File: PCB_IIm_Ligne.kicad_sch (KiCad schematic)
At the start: 24 parts, among them J1 Screw_Terminal_01x08, J2 Screw_Terminal_01x08, J3 Screw_Terminal_01x02, K1 G2RK-2 DC12, K2 Relay_DPDT_Latching_2coil, Q1 IRFZ14, Q2 MPSA56, U2 NE555DR

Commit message: Schematic V1
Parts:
- removed J3: Screw_Terminal_01x02, TerminalBlock_Phoenix:TerminalBlock_Phoenix_MKDS-1,5-2_1x02_P5.00mm_Horizontal, symbol Connector:Screw_Terminal_01x02
- added J4: Screw_Terminal_01x08, TerminalBlock_Phoenix:TerminalBlock_Phoenix_MPT-0,5-8-2.54_1x08_P2.54mm_Horizontal, symbol Connector:Screw_Terminal_01x08
- added J5: Screw_Terminal_01x08, TerminalBlock_Phoenix:TerminalBlock_Phoenix_MKDS-1,5-8-5.08_1x08_P5.08mm_Horizontal, symbol Connector:Screw_Terminal_01x08
- J1, J2: footprint TerminalBlock_Phoenix:TerminalBlock_Phoenix_MKDS-1,5-8-5.08_1x08_P5.08mm_Horizontal -> TerminalBlock_Phoenix:TerminalBlock_Phoenix_MPT-0,5-8-2.54_1x08_P2.54mm_Horizontal
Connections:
- net LED_Traction is gone; now on net LED_Alim: J2.5 (Pin_5)
- net AlimBoutonSens: now also J4.6 (Pin_6)
- net GND: now also J2.2 (Pin_2), J2.3 (Pin_3), J2.4 (Pin_4), J4.1 (Pin_1), J5.1 (Pin_1), J5.2 (Pin_2); no longer J1.1 (Pin_1)
- net LED_Alim: no longer J2.2 (Pin_2)
- net LED_SensA: now also J2.6 (Pin_6); no longer J2.3 (Pin_3)
- net LED_SensB: now also J2.7 (Pin_7); no longer J2.4 (Pin_4)
- net LED_TractionEnService: now also J2.8 (Pin_8)
- net OUT_ARD: now also J4.5 (Pin_5); no longer J1.5 (Pin_5)
- net POT1: now also J4.2 (Pin_2); no longer J1.2 (Pin_2)
- net POT2: now also J4.3 (Pin_3); no longer J1.3 (Pin_3)
- net POT3: now also J4.4 (Pin_4); no longer J1.4 (Pin_4)
- net RAIL_1: now also J5.8 (Pin_8)
- net RAIL_2: now also J5.7 (Pin_7)
- net RelaiBistableSensA: now also J4.7 (Pin_7)
- net RelaiBistableSensB: now also J4.8 (Pin_8)
- net Traction_N: no longer J1.6 (Pin_6)
- net Traction_P: now also J5.3 (Pin_3), J5.4 (Pin_4); no longer J1.7 (Pin_7)
- net VCC: now also J1.8 (Pin_8), J5.5 (Pin_5), J5.6 (Pin_6)
- new net BoutonSensA: J1.5 (Pin_5)
- new net BoutonSensB: J1.4 (Pin_4)
- new net InterrupteurPot1: J1.6 (Pin_6)
- new net InterrupteurPot2: J1.7 (Pin_7)
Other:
- note added: "Connecteur Alimentation"
- note added: "Connecteur Control"
- note added: "Connecteur LED"
- note removed: "A Faire : Importer relai monostable Club Importer relai Bistable Club Importer relai bistable traction Importer Mosfet"
- moved on the sheet: D2, D3, D4, D5, K1, K2, Q2, R1, R2, R3, R5, R6

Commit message: Schematic V2 + BOM
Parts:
- removed C1: 100nF, PCM_JLCPCB:C_0805, symbol PCM_JLCPCB-Capacitors:0805,100nF
- removed C2: 1nF, PCM_JLCPCB:C_0805, symbol PCM_JLCPCB-Capacitors:0805,1nF
- removed D5: D, Diode_THT:D_DO-15_P10.16mm_Horizontal, symbol Device:D
- removed D6, D7: 1N4001W, PCM_JLCPCB:D_SOD-123FL, symbol PCM_JLCPCB-Diodes:General,1N4001W
- removed J5: Screw_Terminal_01x08, TerminalBlock_Phoenix:TerminalBlock_Phoenix_MKDS-1,5-8-5.08_1x08_P5.08mm_Horizontal, symbol Connector:Screw_Terminal_01x08
- removed Q1: IRFZ14, PCM_Package_TO_SOT_THT_AKL:TO-220-3_Vertical_GDS, symbol PCM_Transistor_MOSFET_AKL:IRFZ14
- removed R7: 1kΩ, PCM_JLCPCB:R_0402, symbol PCM_JLCPCB-Resistors:0402,1kΩ
- removed R8: 5.1kΩ, PCM_JLCPCB:R_0603, symbol PCM_JLCPCB-Resistors:0603,5.1kΩ
- removed U2: NE555DR, Package_DIP:DIP-8_W7.62mm_Socket, symbol PCM_JLCPCB-ICs:Timer, 555
- added C1, C5, C6: C100nF, Capacitor_THT:C_Rect_L7.5mm_W6.5mm_P5.00mm, symbol Device:C
- added C2: C1nF, Capacitor_THT:C_Rect_L7.5mm_W6.5mm_P5.00mm, symbol Device:C
- added C3, C4: C_Polarized, symbol Device:C_Polarized
- added D1: D, Diode_THT:D_DO-15_P10.16mm_Horizontal, symbol Device:D
- added J3: Screw_Terminal_01x08, TerminalBlock_Phoenix:TerminalBlock_Phoenix_MKDS-1,5-8-5.08_1x08_P5.08mm_Horizontal, symbol Connector:Screw_Terminal_01x08
- added OC1, OC2, OC3: 6N137, PCM_Package_DIP_AKL:DIP-8_W7.62mm_Socket_LongPads, symbol PCM_Optocoupler_Logic_AKL:6N137
- added Q1: STP80NF12, PCM_Package_TO_SOT_THT_AKL:TO-220-3_Vertical_GDS, symbol PCM_Transistor_MOSFET_AKL:STP80NF12
- added Q3, Q4: IRF9540N, PCM_Package_TO_SOT_THT_AKL:TO-220-3_Vertical_GDS, symbol PCM_Transistor_MOSFET_AKL:IRF9540N
- added R10, R11, R9: R100, Resistor_THT:R_Axial_DIN0207_L6.3mm_D2.5mm_P10.16mm_Horizontal, symbol PCM_Elektuur:R
- added R12, R13, R4, R8: R4.7k, Resistor_THT:R_Axial_DIN0207_L6.3mm_D2.5mm_P10.16mm_Horizontal, symbol PCM_Elektuur:R
- added R14, R15, R16: R, Resistor_THT:R_Axial_DIN0207_L6.3mm_D2.5mm_P10.16mm_Horizontal, symbol PCM_Elektuur:R
- added R7: R1k, Resistor_THT:R_Axial_DIN0207_L6.3mm_D2.5mm_P10.16mm_Horizontal, symbol PCM_Elektuur:R
- added U1: NE555DR, Package_DIP:DIP-8_W7.62mm_Socket, symbol PCM_JLCPCB-ICs:Timer, 555
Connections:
- net BoutonSensA is gone; now on net RelaiBistableSensB: J1.5 (Pin_5)
- net BoutonSensB is gone; now on net RelaiBistableSensA: J1.4 (Pin_4)
- net GATE: now also R9.1 (+)
- net GND: now also C1.2, C2.2, C3.2, C4.2, C5.2, C6.2, D1.2 (A), J3.1 (Pin_1), J3.2 (Pin_2), OC1.3, OC1.5 (GND), OC2.3, OC2.5 (GND), OC3.3, OC3.5 (GND), Q1.2 (D), R4.1 (+), R8.2 (-), U1.1 (GND); no longer D3.2 (A), D4.2 (A)
- net Interrupteur2: now also R4.2 (-)
- net OUT: now also R8.1 (+), U1.3 (OUT)
- net OUT_ARD: now also R16.1 (+); no longer JP1.3 (B)
- net POT1: now also D3.1 (K)
- net POT2: now also D4.2 (A)
- net POT3: now also C1.1, U1.2 (TRIG), U1.6 (THRES)
- net RAIL_1: now also J3.7 (Pin_7)
- net RAIL_2: now also J3.8 (Pin_8)
- net RelaiBistableSensA: now also J1.2 (Pin_2), Q3.2 (D)
- net RelaiBistableSensB: now also J1.3 (Pin_3), D1.1 (K), Q4.2 (D); no longer D3.1 (K), D4.1 (K)
- net Traction_N: now also Q1.3 (S)
- net Traction_P: now also C4.1, J3.3 (Pin_3), J3.4 (Pin_4)
- net VCC: now also C3.1, C5.1, C6.1, J3.5 (Pin_5), J3.6 (Pin_6), OC1.7 (EN), OC1.8 (VCC), OC2.8 (VCC), OC3.8 (VCC), Q3.3 (S), Q4.3 (S), R12.2 (-), R13.2 (-), R7.1 (+), U1.4 (RST), U1.8 (VCC)
- new net: C2.1, U1.5 (CONT)
- new net: Q4.1 (G), R11.2 (-), R13.1 (+)
- new net: OC3.2, R16.2 (-)
- new net: Q1.1 (G), R9.2 (-)
- new net: D3.2 (A), D4.1 (K), R7.2 (-), U1.7 (DISCH)
- new net: Q3.1 (G), R10.2 (-), R12.1 (+)
- new net: OC2.2, R15.2 (-)
- new net: OC2.6, R11.1 (+)
- new net: OC1.2, R14.2 (-)
- new net: OC1.6, R10.1 (+)
- new net CommandeSensA: R14.1 (+)
- new net CommandeSensB: R15.1 (+)
- new net CommandeTractionArduino: JP1.3 (B), OC3.6
- no-connect marks 0 -> 2
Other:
- moved on the sheet: JP1, K2

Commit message: Schematic V1
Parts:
- removed C1: C100nF, Capacitor_THT:C_Rect_L7.5mm_W6.5mm_P5.00mm, symbol Device:C
- removed C2: C1nF, Capacitor_THT:C_Rect_L7.5mm_W6.5mm_P5.00mm, symbol Device:C
- removed OC2, OC3: 6N137, PCM_Package_DIP_AKL:DIP-8_W7.62mm_Socket_LongPads, symbol PCM_Optocoupler_Logic_AKL:6N137
- removed Q1: STP80NF12, PCM_Package_TO_SOT_THT_AKL:TO-220-3_Vertical_GDS, symbol PCM_Transistor_MOSFET_AKL:STP80NF12
- removed Q3, Q4: IRF9540N, PCM_Package_TO_SOT_THT_AKL:TO-220-3_Vertical_GDS, symbol PCM_Transistor_MOSFET_AKL:IRF9540N
- removed R16: R, Resistor_THT:R_Axial_DIN0207_L6.3mm_D2.5mm_P10.16mm_Horizontal, symbol PCM_Elektuur:R
- removed R9: R100, Resistor_THT:R_Axial_DIN0207_L6.3mm_D2.5mm_P10.16mm_Horizontal, symbol PCM_Elektuur:R
- removed U1: NE555DR, Package_DIP:DIP-8_W7.62mm_Socket, symbol PCM_JLCPCB-ICs:Timer, 555
- added C7: C100nF, Capacitor_THT:C_Rect_L7.5mm_W6.5mm_P5.00mm, symbol Device:C
- added C8: C_Polarized, symbol Device:C_Polarized
- added DZ1: 1N4733A, PCM_Diode_THT_AKL:D_DO-41_SOD81_P10.16mm_Horizontal_Zener, symbol PCM_Diode_Zener_AKL:1N4733A
- added JP2: SolderJumper_2_Bridged, Jumper:SolderJumper-2_P1.3mm_Bridged_RoundedPad1.0x1.5mm, symbol Jumper:SolderJumper_2_Bridged
- added Q3, Q4: BC557B, PCM_Package_TO_SOT_THT_AKL:TO-92_Inline_Wide_CBE, symbol PCM_Transistor_BJT_AKL:BC557B
- added Q5: 2N3904, PCM_Package_TO_SOT_THT_AKL:TO-92_Inline_Wide_EBC, symbol PCM_Transistor_BJT_AKL:2N3904
- added Q6: IRF40B207, PCM_Package_TO_SOT_THT_AKL:TO-220-3_Vertical_GDS, symbol PCM_Transistor_MOSFET_AKL:IRF40B207
- added U2: TLC555xP, PCM_Package_DIP_AKL:DIP-8_W7.62mm_LongPads, symbol Timer:TLC555xP
- C6: value C100nF -> C1nF
- OC1: footprint PCM_Package_DIP_AKL:DIP-8_W7.62mm_Socket_LongPads -> PCM_Package_DIP_AKL:DIP-8_W7.62mm_LongPads
- R10, R11: value R100 -> R
- R12, R8: value R4.7k -> R1k
- R13: value R4.7k -> R10k
- R14: value R -> R10k
- R15: value R -> R100
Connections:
- net CommandeSensB is gone; now on an unnamed net: R15.1 (+)
- net GND: now also J3.7 (Pin_7), J3.8 (Pin_8), R13.1 (+), C7.2, C8.2, DZ1.2 (A), U2.1 (GND); no longer J3.1 (Pin_1), J3.2 (Pin_2), OC1.3, R8.2 (-)
- net OUT: no longer R8.1 (+)
- net POT3: now also C5.1, U2.2 (TR), U2.6 (THR)
- net RAIL_1: now also J3.6 (Pin_6); no longer J3.7 (Pin_7)
- net RAIL_2: now also J3.5 (Pin_5); no longer J3.8 (Pin_8)
- net RelaiBistableSensA: now also Q3.1 (C)
- net RelaiBistableSensB: now also Q4.1 (C)
- net Traction_P: now also Q6.3 (S); no longer J3.3 (Pin_3), J3.4 (Pin_4)
- net VCC: now also J3.1 (Pin_1), J3.2 (Pin_2), R14.2 (-), R8.1 (+), C7.1, C8.1, Q3.3 (E), Q4.3 (E), Q5.3 (C), U2.4 (R), U2.8 (VCC); no longer C5.1, C6.1, J3.5 (Pin_5), J3.6 (Pin_6), OC1.7 (EN), OC1.8 (VCC), R12.2 (-), R13.2 (-)
- net at R11.2 (-): now also Q4.2 (B); no longer R13.1 (+)
- net at D3.2 (A), D4.1 (K), R7.2 (-): now also U2.7 (DIS)
- net at R12.1 (+): now also OC1.6; no longer R10.2 (-)
- net at R15.2 (-): now also Q6.1 (G)
- net CommandeRelaiArdB: now reaches R11.1 (+)
- net at OC1.2: no longer R14.2 (-)
- net CommandeRelaiArdA: now reaches R10.1 (+)
- net CommandeRelaiArdA: no longer OC1.6
- net CommandeSensA: no longer names the net of R14.1 (+)
- net CommandeSensA: now also Q5.1 (E)
- net Traction_N: no longer names the net of K1.3
- net Traction_N: no longer K1.6
- new net: C6.1, U2.5 (CV)
- new net: Q5.2 (B), R12.2 (-), R13.2 (-)
- new net: Q3.2 (B), R10.2 (-)
- new net: JP2.1 (A), OC1.7 (EN)
- new net +20V: J3.3 (Pin_3), J3.4 (Pin_4), Q6.2 (D)
- new net +5V: DZ1.1 (K), JP2.2 (B), OC1.8 (VCC), R8.2 (-)
- no-connect marks 2 -> 0
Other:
- note added: "Commande Relai Via Arduino - Transistor P"
- moved on the sheet: D3, D4, J3, R7

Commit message: Schematic V2
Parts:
- removed DZ1: 1N4733A, PCM_Diode_THT_AKL:D_DO-41_SOD81_P10.16mm_Horizontal_Zener, symbol PCM_Diode_Zener_AKL:1N4733A
- removed JP2: SolderJumper_2_Bridged, Jumper:SolderJumper-2_P1.3mm_Bridged_RoundedPad1.0x1.5mm, symbol Jumper:SolderJumper_2_Bridged
- removed OC1: 6N137, PCM_Package_DIP_AKL:DIP-8_W7.62mm_LongPads, symbol PCM_Optocoupler_Logic_AKL:6N137
- removed R8: R1k, Resistor_THT:R_Axial_DIN0207_L6.3mm_D2.5mm_P10.16mm_Horizontal, symbol PCM_Elektuur:R
- added H1, H2, H3, H4: MountingHole, MountingHole:MountingHole_3.2mm_M3, symbol Mechanical:MountingHole
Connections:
- net GND: now also K1.3, K1.6
- net CommandetTraction: now reaches U2.3 (Q)
- net CommandetTraction: now also R12.1 (+)
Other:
- moved on the sheet: R7

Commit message: Schematic V1
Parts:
- removed C8: C_Polarized, symbol Device:C_Polarized
- removed Q3, Q4: BC557B, PCM_Package_TO_SOT_THT_AKL:TO-92_Inline_Wide_CBE, symbol PCM_Transistor_BJT_AKL:BC557B
- removed Q5: 2N3904, PCM_Package_TO_SOT_THT_AKL:TO-92_Inline_Wide_EBC, symbol PCM_Transistor_BJT_AKL:2N3904
- removed R11: R, Resistor_THT:R_Axial_DIN0207_L6.3mm_D2.5mm_P10.16mm_Horizontal, symbol PCM_Elektuur:R
- removed R3: R4.7k, Resistor_THT:R_Axial_DIN0207_L6.3mm_D2.5mm_P10.16mm_Horizontal, symbol PCM_Elektuur:R
- added JP3, JP4: SolderJumper_2_Bridged, symbol Jumper:SolderJumper_2_Bridged
- added Q7, Q8, Q9: 2N2222A, PCM_Package_TO_SOT_THT_AKL:TO-92_Inline_Wide_EBC, symbol PCM_Transistor_BJT_AKL:2N3904
- added R18, R9: 260, Resistor_THT:R_Axial_DIN0207_L6.3mm_D2.5mm_P10.16mm_Horizontal, symbol PCM_Elektuur:R
- added R19, R8: 10k, Resistor_THT:R_Axial_DIN0207_L6.3mm_D2.5mm_P10.16mm_Horizontal, symbol PCM_Elektuur:R
- C5: value C100nF -> 270nF
- C7: value C100nF -> 100nF
- R10: value R -> 10k
- R12: value R1k -> 1K
- R15: value R100 -> 1K
- R4: value R4.7k -> 220
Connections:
- net CommandeRelaiArdA is gone; now on net GND: R10.1 (+)
- net Interrupteur2 is gone; now on net Interrupteur: R4.2 (-), R6.1 (+)
- net GND: now also JP3.1 (A), JP4.1 (A), Q7.1 (E), Q8.1 (E), Q9.1 (E), R19.1 (+), R8.2 (-); no longer K2.15, K2.16
- net VCC: no longer U2.4 (R)
- net Interrupteur: now reaches Q2.2 (B)
- net Interrupteur: now also U2.4 (R), R8.1 (+)
- net at R12.2 (-), R13.2 (-): now also Q9.2 (B)
- net at R10.2 (-): now also Q8.2 (B), R9.2 (-)
- net at R15.1 (+): now also Q9.3 (C); no longer R14.1 (+)
- net at Q6.1 (G), R15.2 (-): now also R14.1 (+)
- net InterrupteurPot2: no longer names the net of J1.7 (Pin_7)
- new net: Q7.2 (B), R18.2 (-), R19.2 (-)
- new net RelaiBistableSensA_N: JP3.2 (B), JP4.2 (B), K2.15, K2.16, Q7.3 (C), Q8.3 (C)
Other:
- note removed: "Commande Relai Via Arduino - Transistor P"
- moved on the sheet: C5, C6, C7, D3, D4, Q6, R12, R13, R14, R15, R4, R7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

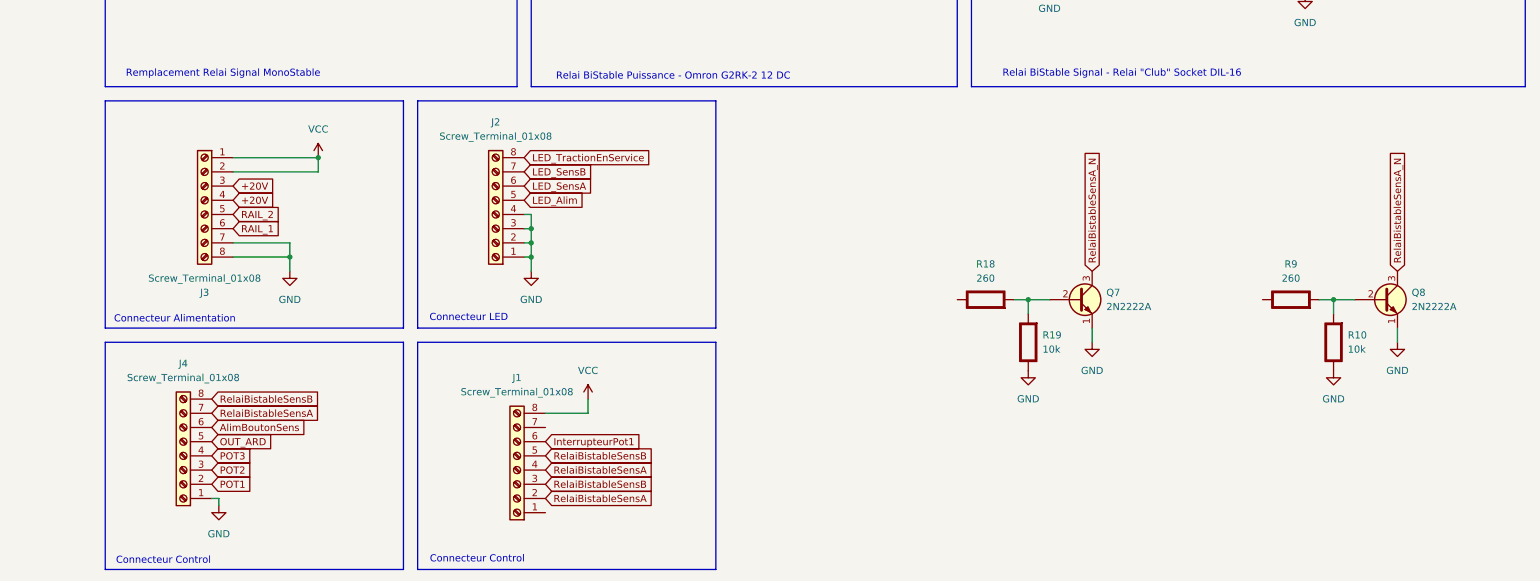
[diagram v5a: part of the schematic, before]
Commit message: Schematic Modification
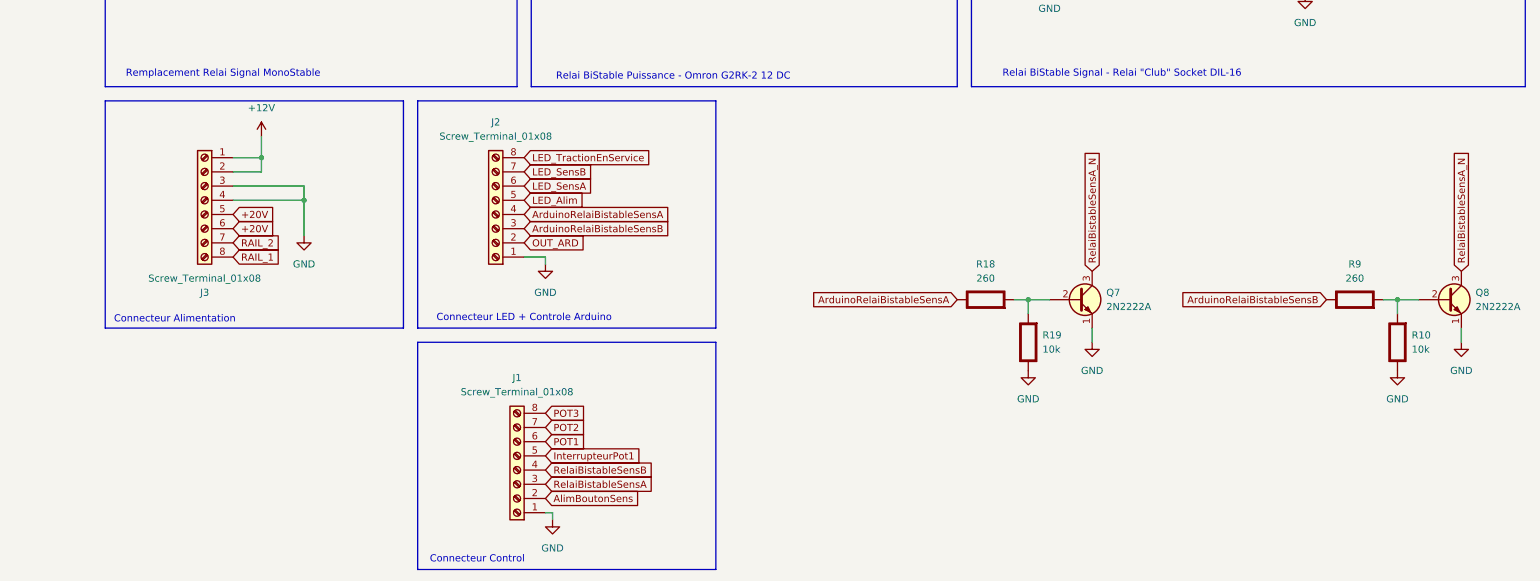
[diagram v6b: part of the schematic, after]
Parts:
- removed J4: Screw_Terminal_01x08, TerminalBlock_Phoenix:TerminalBlock_Phoenix_MPT-0,5-8-2.54_1x08_P2.54mm_Horizontal, symbol Connector:Screw_Terminal_01x08
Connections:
- net +20V: now also J3.5 (Pin_5), J3.6 (Pin_6); no longer J3.3 (Pin_3), J3.4 (Pin_4)
- net AlimBoutonSens: now also J1.2 (Pin_2)
- net GND: now also J1.1 (Pin_1), J3.3 (Pin_3), J3.4 (Pin_4); no longer J2.2 (Pin_2), J2.3 (Pin_3), J2.4 (Pin_4), J3.7 (Pin_7), J3.8 (Pin_8)
- net InterrupteurPot1: now also J1.5 (Pin_5); no longer J1.6 (Pin_6)
- net OUT_ARD: now also J2.2 (Pin_2)
- net POT1: now also J1.6 (Pin_6)
- net POT2: now also J1.7 (Pin_7)
- net POT3: now also J1.8 (Pin_8)
- net RAIL_1: now also J3.8 (Pin_8); no longer J3.6 (Pin_6)
- net RAIL_2: now also J3.7 (Pin_7); no longer J3.5 (Pin_5)
- net RelaiBistableSensA: now also J1.3 (Pin_3); no longer J1.2 (Pin_2), J1.4 (Pin_4)
- net RelaiBistableSensB: now also J1.4 (Pin_4); no longer J1.3 (Pin_3), J1.5 (Pin_5)
- net VCC: no longer J1.8 (Pin_8), J3.1 (Pin_1), J3.2 (Pin_2)
- net ArduinoRelaiBistableSensB: now reaches R9.1 (+)
- net ArduinoRelaiBistableSensB: now also J2.3 (Pin_3)
- net ArduinoRelaiBistableSensA: now reaches R18.1 (+)
- net ArduinoRelaiBistableSensA: now also J2.4 (Pin_4)
- new net +12V: J3.1 (Pin_1), J3.2 (Pin_2)
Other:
- note added: "Connecteur LED + Controle Arduino"
- note removed: "Connecteur LED"
- moved on the sheet: Q8, R10, R9
